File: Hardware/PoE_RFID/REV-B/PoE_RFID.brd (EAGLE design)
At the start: 102 x 62.1 mm, 98 parts, among them IC2 ATMEGA32U4-MU, J6 10103594-0001LF, SW1 SPST_TACT-KMR2, U1 PN532, U2 SPX3819-3.3, U3 74AHC1G125, U4 W5500, X2 J1011FHANRUN, Y1 27.12MHz, Y4 8MHz

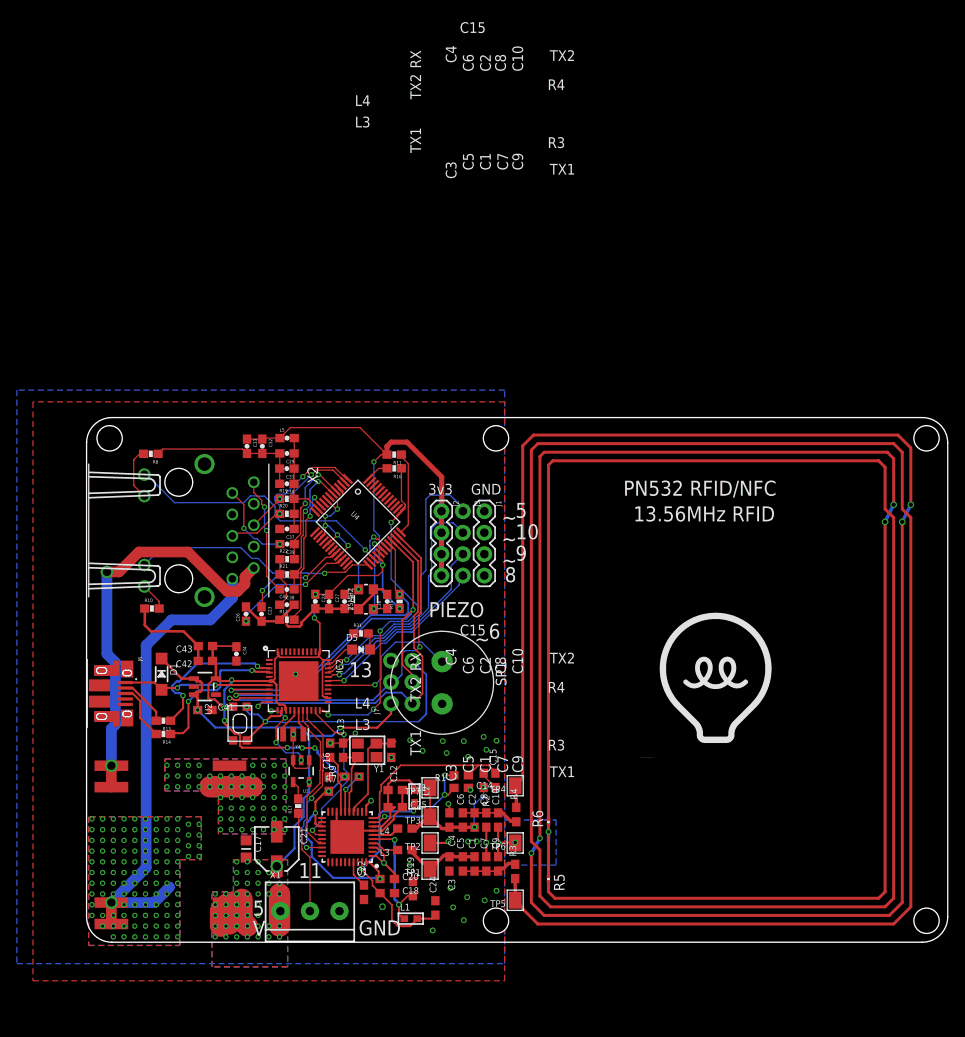
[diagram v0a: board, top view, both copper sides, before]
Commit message: HEEP-615 added reset pulllup
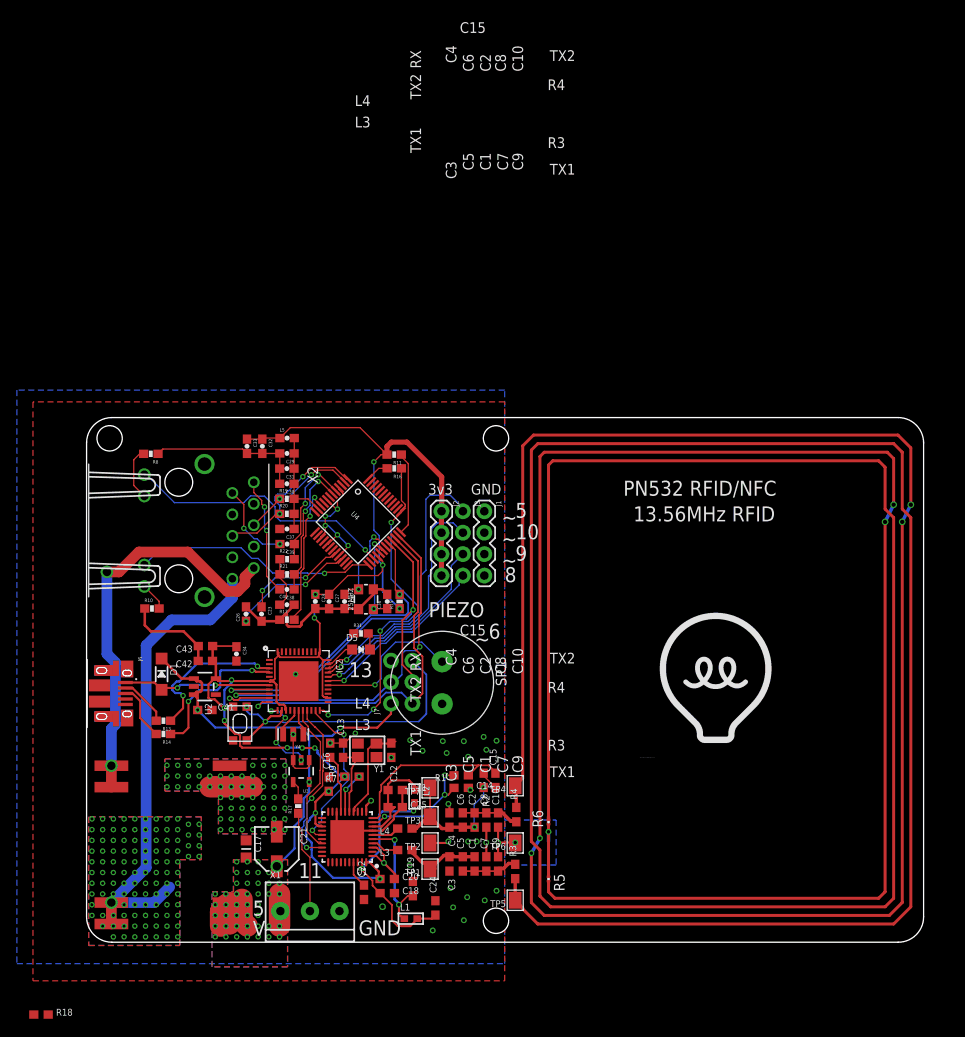
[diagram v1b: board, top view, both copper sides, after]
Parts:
- added R18: 10K, microbuilder:0603-NO
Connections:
- net +3V3: now also R18.2
- net RSTPD_N: now also R18.1
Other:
- board size 102 x 62.1 mm -> 99.2 x 62.1 mm
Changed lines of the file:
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@@
 <?xml version="1.0" encoding="utf-8"?>
 <!DOCTYPE eagle SYSTEM "eagle.dtd">
-<eagle version="8.4.3">
+<eagle version="8.5.0">
 <drawing>
 <settings>
@@
 <setting verticaltext="up"/>
 </settings>
-<grid distance="0.15875" unitdist="mm" unit="mm" style="lines" multiple="1" display="no" altdistance="0.025" altunitdist="inch" altunit="mm"/>
+<grid distance="0.3175" unitdist="mm" unit="mm" style="lines" multiple="1" display="no" altdistance="0.025" altunitdist="inch" altunit="mm"/>
 <layers>
 <layer number="1" name="Top" color="4" fill="1" visible="yes" active="yes"/>
@@
 <layer number="14" name="Route14" color="1" fill="6" visible="no" active="no"/>
 <layer number="15" name="Route15" color="4" fill="6" visible="no" active="no"/>
-<layer number="16" name="Bottom" color="1" fill="1" visible="no" active="yes"/>
+<layer number="16" name="Bottom" color="1" fill="1" visible="yes" active="yes"/>
 <layer number="17" name="Pads" color="2" fill="1" visible="yes" active="yes"/>
 <layer number="18" name="Vias" color="2" fill="1" visible="yes" active="yes"/>
-<layer number="19" name="Unrouted" color="11" fill="4" visible="no" active="yes"/>
-<layer number="20" name="Dimension" color="15" fill="1" visible="no" active="yes"/>
-<layer number="21" name="tPlace" color="6" fill="1" visible="no" active="yes"/>
+<layer number="19" name="Unrouted" color="11" fill="4" visible="yes" active="yes"/>
+<layer number="20" name="Dimension" color="15" fill="1" visible="yes" active="yes"/>
+<layer number="21" name="tPlace" color="6" fill="1" visible="yes" active="yes"/>
 <layer number="22" name="bPlace" color="7" fill="1" visible="no" active="yes"/>
-<layer number="23" name="tOrigins" color="15" fill="1" visible="no" active="yes"/>
+<layer number="23" name="tOrigins" color="15" fill="1" visible="yes" active="yes"/>
 <layer number="24" name="bOrigins" color="15" fill="1" visible="no" active="yes"/>
 <layer number="25" name="tNames" color="7" fill="1" visible="no" active="yes"/>
 <layer number="26" name="bNames" color="7" fill="1" visible="no" active="yes"/>
-<layer number="27" name="tValues" color="7" fill="1" visible="yes" active="yes"/>
+<layer number="27" name="tValues" color="7" fill="1" visible="no" active="yes"/>
 <layer number="28" name="bValues" color="7" fill="1" visible="no" active="yes"/>
 <layer number="29" name="tStop" color="7" fill="3" visible="no" active="yes"/>
@@
 <layer number="43" name="vRestrict" color="2" fill="10" visible="no" active="yes"/>
 <layer number="44" name="Drills" color="7" fill="1" visible="no" active="yes"/>
-<layer number="45" name="Holes" color="7" fill="1" visible="no" active="yes"/>
-<layer number="46" name="Milling" color="3" fill="1" visible="no" active="yes"/>
+<layer number="45" name="Holes" color="7" fill="1" visible="yes" active="yes"/>
+<layer number="46" name="Milling" color="3" fill="1" visible="yes" active="yes"/>
 <layer number="47" name="Measures" color="7" fill="1" visible="no" active="yes"/>
 <layer number="48" name="Document" color="7" fill="1" visible="no" active="yes"/>
 <layer number="49" name="Reference" color="7" fill="1" visible="no" active="yes"/>
 <layer number="50" name="dxf" color="7" fill="1" visible="no" active="yes"/>
-<layer number="51" name="tDocu" color="7" fill="1" visible="no" active="yes"/>
+<layer number="51" name="tDocu" color="7" fill="1" visible="yes" active="yes"/>
 <layer number="52" name="bDocu" color="7" fill="1" visible="no" active="yes"/>
 <layer number="53" name="tGND_GNDA" color="7" fill="9" visible="no" active="no"/>
@@
 <board>
 <plain>
-<wire x1="3" y1="0" x2="98.9975" y2="0" width="0" layer="20"/>
-<wire x1="102.0125" y1="3" x2="102.0125" y2="59.15" width="0" layer="20"/>
-<wire x1="98.9975" y1="62.15" x2="3" y2="62.15" width="0" layer="20"/>
+<wire x1="3" y1="0" x2="96.14" y2="0" width="0" layer="20"/>
+<wire x1="99.155" y1="3" x2="99.155" y2="59.15" width="0" layer="20"/>
+<wire x1="96.14" y1="62.15" x2="3" y2="62.15" width="0" layer="20"/>
 <wire x1="0" y1="59.15" x2="0" y2="3" width="0" layer="20"/>
-<wire x1="102.0125" y1="3" x2="98.9975" y2="0" width="0" layer="20" curve="-90.003801"/>
-<wire x1="102.0125" y1="59.15" x2="98.9975" y2="62.15" width="0" layer="20" curve="90.003801"/>
+<wire x1="99.155" y1="3" x2="96.14" y2="0" width="0" layer="20" curve="-90.003801"/>
+<wire x1="99.155" y1="59.15" x2="96.14" y2="62.15" width="0" layer="20" curve="90.003801"/>
 <wire x1="3" y1="0" x2="0" y2="3" width="0" layer="20" curve="-90"/>
 <wire x1="3" y1="62.15" x2="0" y2="59.15" width="0" layer="20" curve="90"/>
@@
 <text x="32.221340625" y="0.813528125" size="1.778" layer="21">GND</text>
 <text x="40.52945625" y="38.5092375" size="1.778" layer="21">PIEZO</text>
-<hole x="99.5" y="2.54" drill="3"/>
-<hole x="99.5" y="59.69" drill="3"/>
 <text x="25.104125" y="7.601421875" size="1.778" layer="21">11</text>
 <text x="47.629165625" y="35.94859375" size="1.778" layer="21">6</text>
@@
 <param name="checkRestrict" value="0"/>
 <param name="checkStop" value="0"/>
+<param name="checkValues" value="0"/>
 <param name="useDiameter" value="13"/>
 <param name="maxErrors" value="50"/>
@@
 <attribute name="VALUE" x="42.549234375" y="52.324" size="0.6096" layer="27" font="vector" ratio="20" rot="R270"/>
 </element>
+<element name="R18" library="microbuilder" package="0603-NO" value="10K" x="-5.3975" y="-8.5725"/>
 </elements>
 <signals>
@@
 <wire x1="42.070303125" y1="55.1208875" x2="42.070303125" y2="51.08306875" width="0.6096" layer="1"/>
 <wire x1="42.070303125" y1="51.08306875" x2="42.041234375" y2="51.054" width="0.6096" layer="1"/>
+<contactref element="R18" pad="2"/>
+<wire x1="-4.5475" y1="-8.5725" x2="26.67" y2="10.16" width="0" layer="19" extent="1-16"/>
 </signal>
 <signal name="13">
@@
 <signal name="RSTPD_N">
 <contactref element="U1" pad="38"/>
+<contactref element="R18" pad="1"/>
+<wire x1="-6.2475" y1="-8.5725" x2="32.1275" y2="9.474" width="0" layer="19" extent="1-1"/>
 </signal>
 <signal name="TX1_ANTENNA">

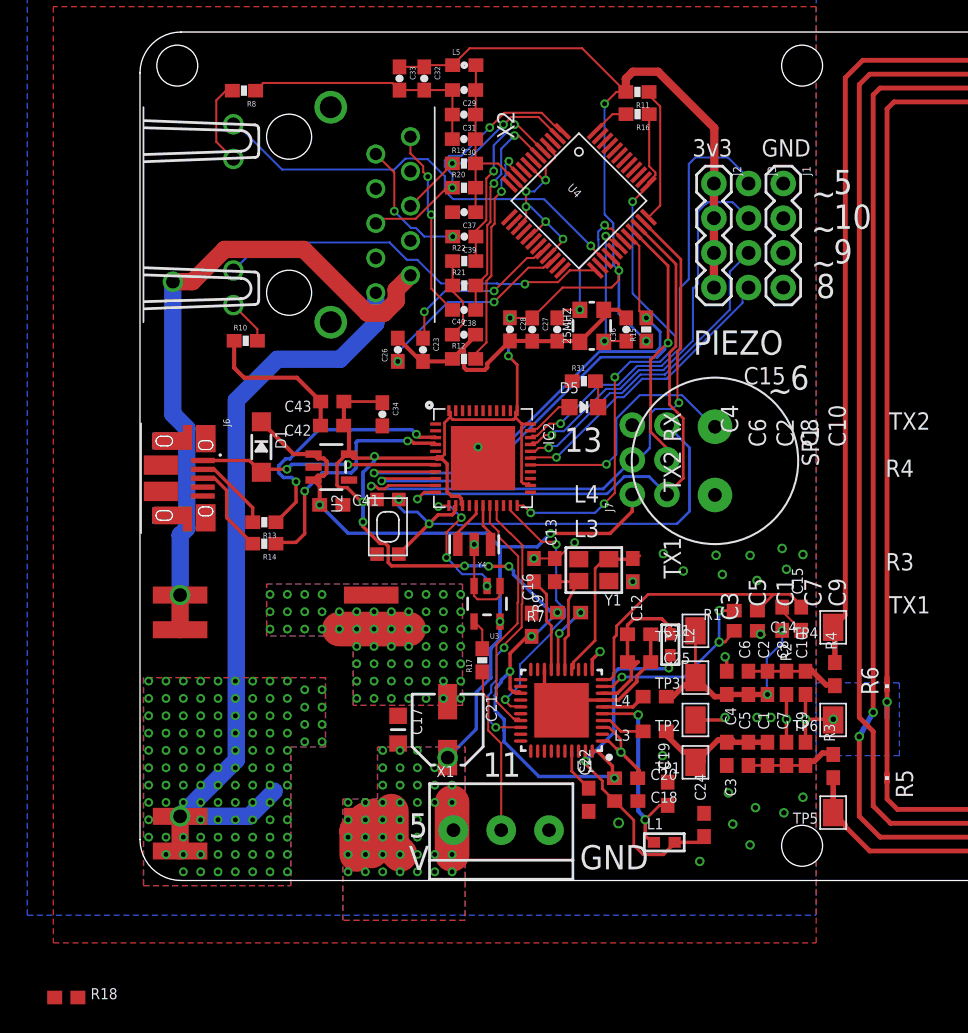
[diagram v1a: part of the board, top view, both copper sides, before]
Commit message: HEEP-615 added eagle backup files to gitignore, added pin 1 indicator to PoE module. more progress on RFID pcb layout
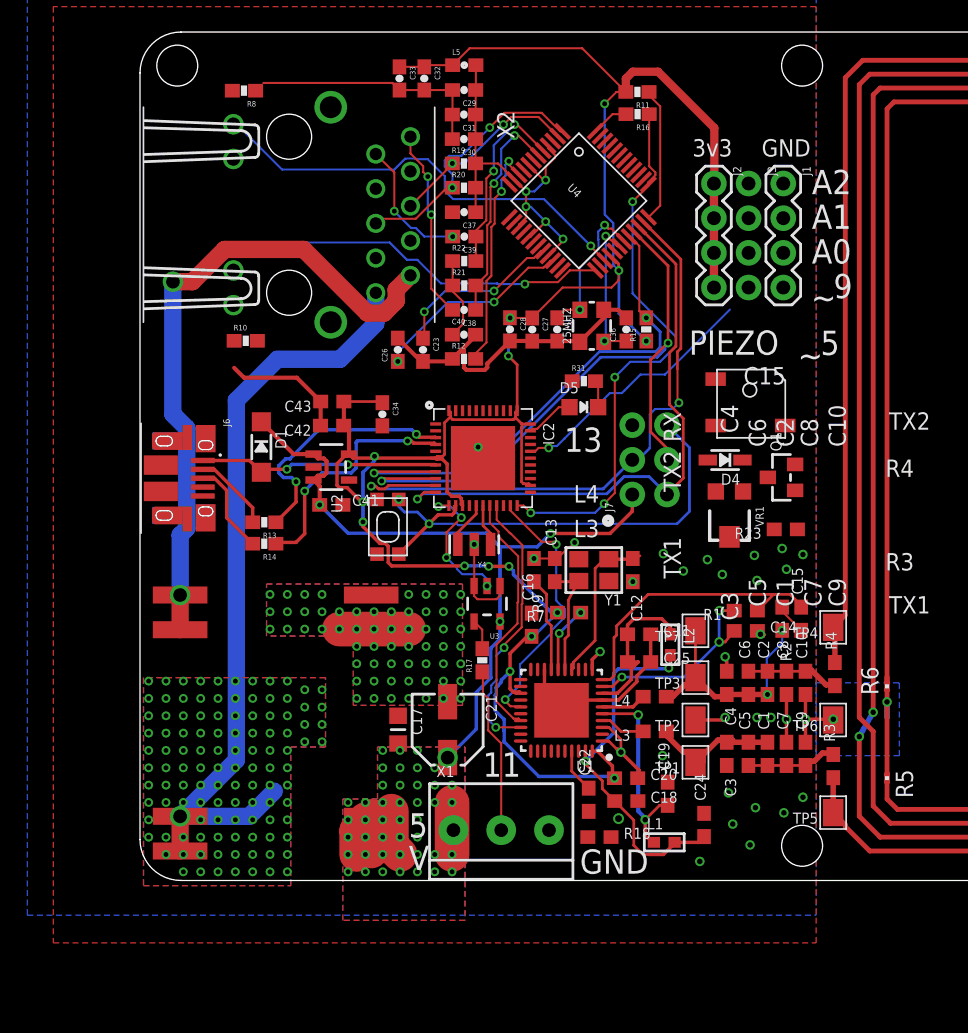
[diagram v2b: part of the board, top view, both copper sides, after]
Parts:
- removed SP1: SPEAKER/PS12, microbuilder:PS12
- added D4: 1N4148, microbuilder:SOD-323
- added Q1: MMBT2222, microbuilder:SOT23-WIDE
- added R23: 100, microbuilder:0603-NO
- added SP2: 8MM - KLJ-5030, microbuilder:BUZZER_SMT_5MM
- added VR1: 1k, SparkFun-Resistors:TRIMPOT-SMD-TC33X
- moved R18 40.8 mm to (33.7, 3.17)
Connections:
- removed net 0: IC2.20
- removed net 5_PWM: IC2.31, J3.1
- removed net EN3: IC2.27, SP1.P$1
- new net 3.3V: D4.C, SP2.-
- new net N$29: Q1.1, R23.1
- new net N$30: D4.A, Q1.3, SP2.+
- new net N$31: R23.2, VR1.2
- new net SPEAKER: IC2.31, VR1.3
- net +3V3: now also R10.1, R8.1
- net 10_PWM: no longer J3.2
- net 9_PWM: now also J3.4; no longer J3.3
- net A0: now also J3.3
- net A1: now also J3.2
- net A2: now also J3.1
- net ACTLED: now also X2.12; no longer X2.11
- net D8: no longer J3.4
- net GND: now also Q1.2; no longer R10.1, R8.1, SP1.P$2
- net LNKLED: now also X2.14; no longer X2.13
- net N$27: now also R8.2, X2.11; no longer R10.2, X2.14
- net N$28: now also R10.2, X2.13; no longer R8.2, X2.12
- net RSTPD_N: now also IC2.20
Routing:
- net 5_PWM: track 33.0 -> 0.00 mm, vias 1 -> 0
- net 10_PWM: track 29.2 -> 0.00 mm, vias 1 -> 0
- net D8: track 21.8 -> 0.00 mm, vias 1 -> 0
- net EN3: track 18.1 -> 0.00 mm, vias 1 -> 0
- net N$28: track 6.29 -> 0.00 mm
- net 9_PWM: track 23.7 -> 19.0 mm
- net N$27: track 3.34 -> 0.00 mm
- net LNKLED: track 29.0 -> 26.1 mm
- net GND: track 117.5 -> 114.7 mm
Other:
- board text added: "A0"
- board text added: "A1"
- board text added: "A2"
- board text removed: "10"
- board text removed: "6"
- board text removed: "8"

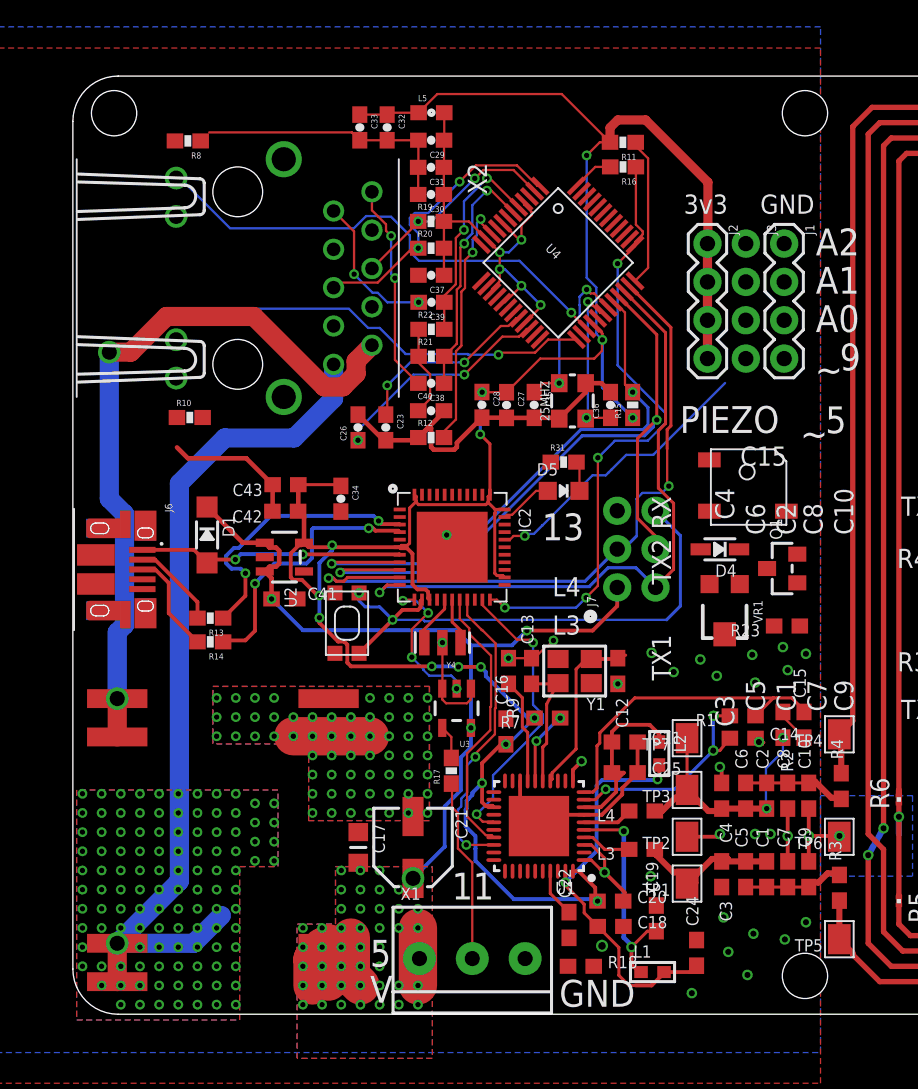
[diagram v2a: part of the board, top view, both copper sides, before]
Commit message: HEEP-615 shrunk microusb holes to prevent wiggle. PCB for dylan to review
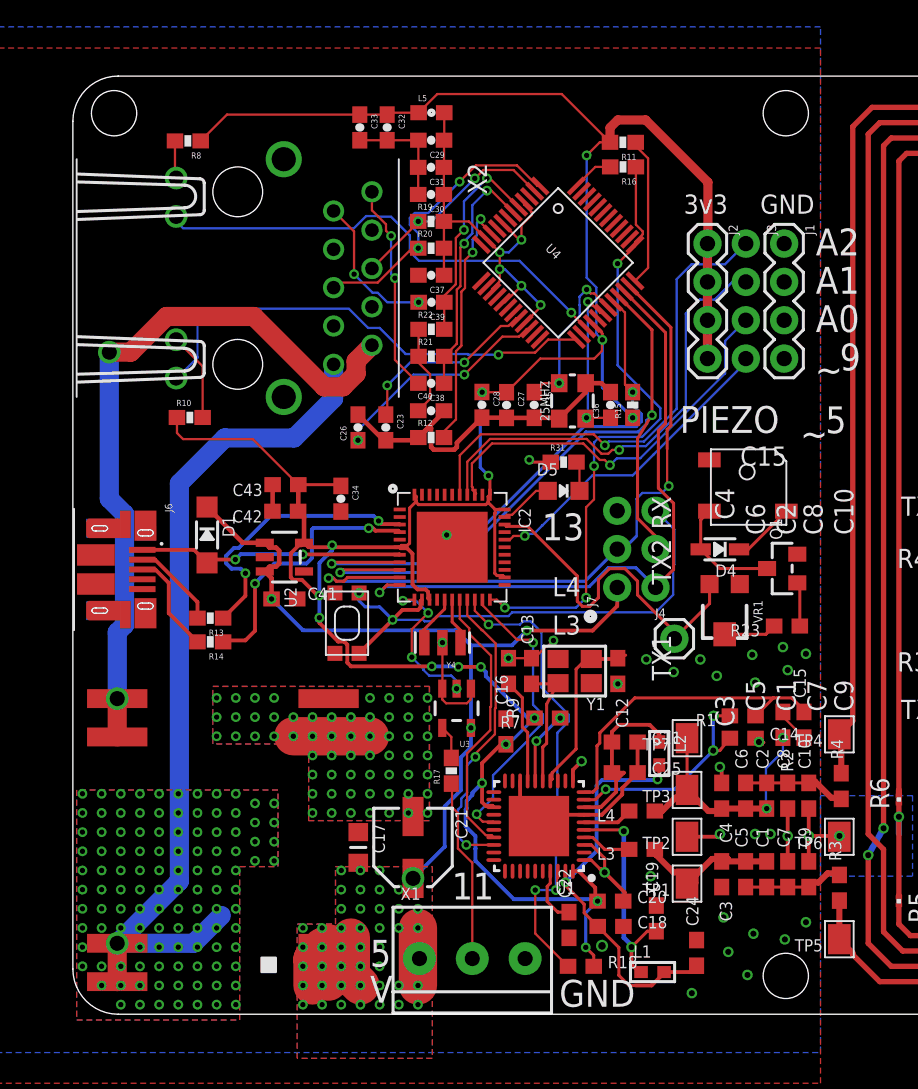
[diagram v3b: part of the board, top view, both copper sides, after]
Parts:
- added J4: (no value), SparkFun-Connectors:1X01
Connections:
- net SPEAKER: now also J4.1
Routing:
- net A2: track 0.00 -> 33.0 mm, vias 0 -> 1
- net RSTPD_N: track 0.00 -> 32.7 mm, vias 0 -> 3
- net A1: track 0.00 -> 30.0 mm, vias 0 -> 1
- net A0: track 0.00 -> 26.7 mm, vias 0 -> 1
- net +3V3: track 169.5 -> 196.1 mm, vias 15 -> 16
- net SPEAKER: track 0.00 -> 23.5 mm
- net GND: track 114.7 -> 98.6 mm, vias 94 -> 95
- net N$30: track 0.00 -> 7.69 mm
- net N$28: track 0.00 -> 5.88 mm
- net LNKLED: track 26.1 -> 31.6 mm
- net 3.3V: track 0.00 -> 4.18 mm
- net N$31: track 0.00 -> 3.50 mm
- net N$29: track 0.00 -> 2.93 mm
- net N$27: track 0.00 -> 2.49 mm
- net 9_PWM: track 19.0 -> 21.1 mm
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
